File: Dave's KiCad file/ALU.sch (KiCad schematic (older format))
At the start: 0 parts

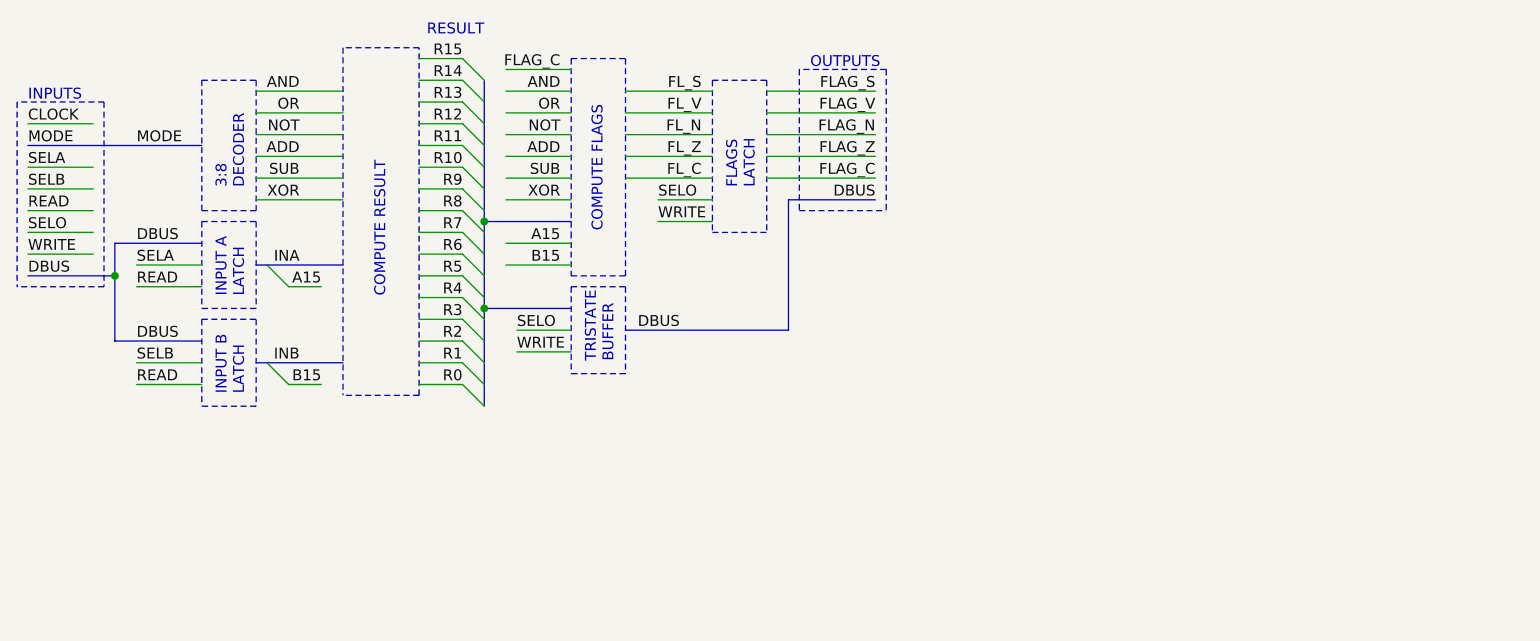
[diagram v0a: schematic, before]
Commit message: Remove READ and WRITE
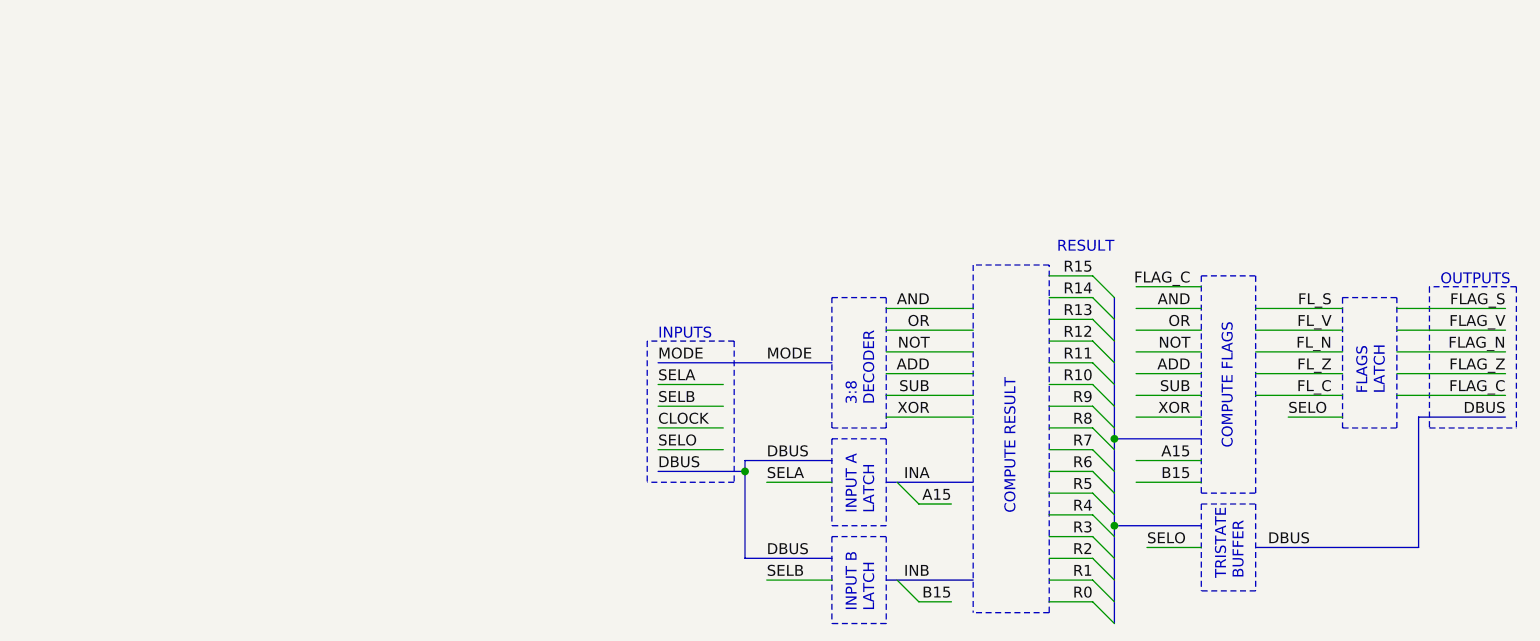
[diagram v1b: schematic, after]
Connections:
- net labels removed: READ, WRITE
- wire segments 57 -> 51
